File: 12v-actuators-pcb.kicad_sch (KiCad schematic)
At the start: 17 parts, among them J2 3.5mm WR-TBL, J3 690367280676, J5 65100516121, J7 RGBA_LEDs, J8 CAN, U1 MCP2551-I-SN

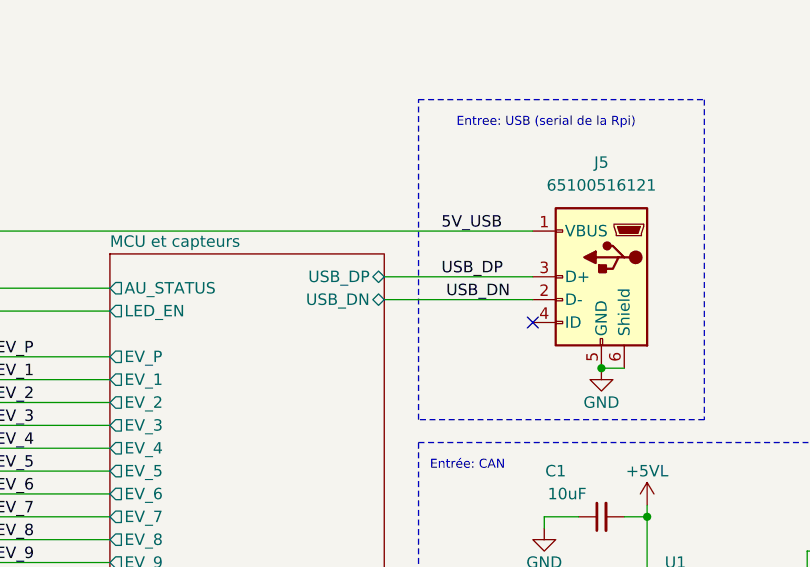
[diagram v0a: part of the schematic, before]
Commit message: debut du tracee des pistes (et modification de l'empreinte R_0402_1005Metric_jumperClosed.kicad_mod pour que le DRC accepte de la router
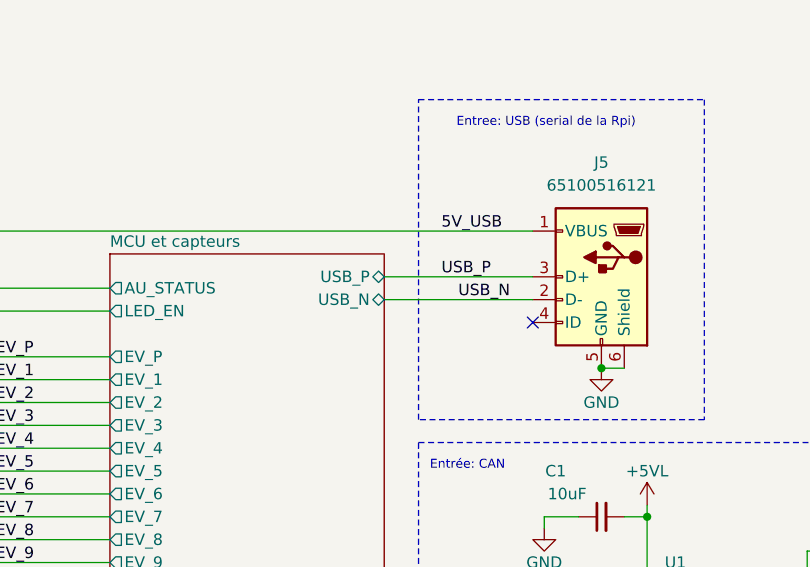
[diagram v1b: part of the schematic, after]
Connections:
- net USB_DN renamed USB_N
- net USB_DP renamed USB_P
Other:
- sheet MCU et capteurs ports: added USB_N, USB_P; removed USB_DN, USB_DP
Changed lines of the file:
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@@
 		)
 	)
-	(label "USB_DN"
+	(label "USB_N"
 		(at 193.04 74.93 180)
 		(effects
@@
 		)
 	)
-	(label "USB_DP"
+	(label "USB_P"
 		(at 185.42 72.39 0)
 		(effects
@@
 			)
 		)
-		(pin "USB_DP" bidirectional
+		(pin "USB_P" bidirectional
 			(at 179.07 72.39 0)
 			(effects
@@
 			)
 		)
-		(pin "USB_DN" bidirectional
+		(pin "USB_N" bidirectional
 			(at 179.07 74.93 0)
 			(effects

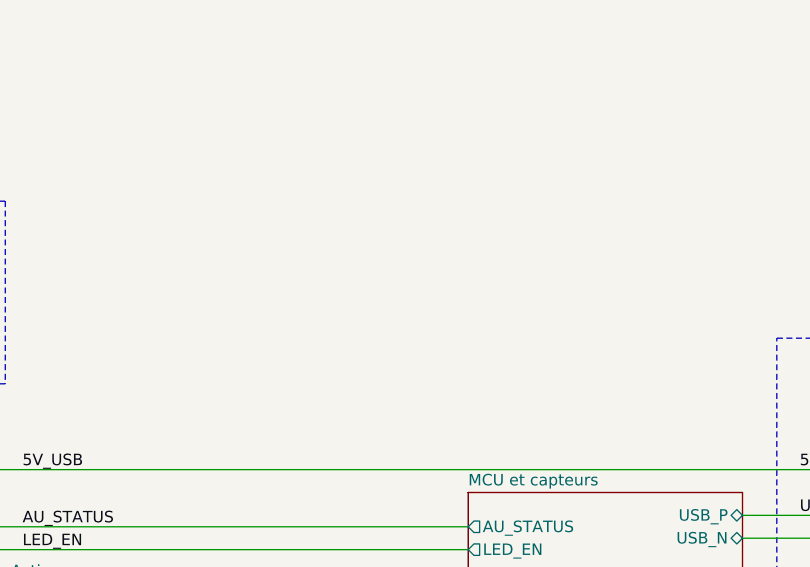
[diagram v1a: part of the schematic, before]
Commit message: WIP ajout des carte Mini-PAMI au routage (todo: finir routage, repeter, associer ref JLCPCB, enregistrer empreinte OPB620 et TRIMM)
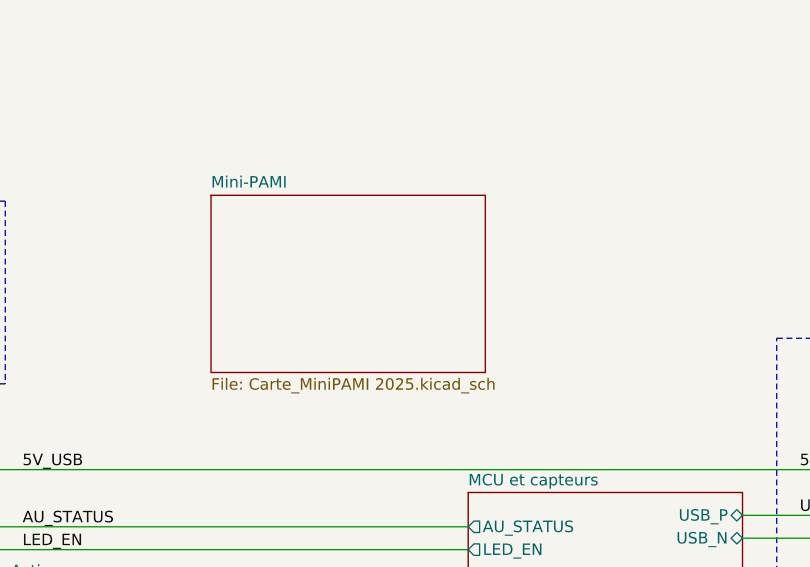
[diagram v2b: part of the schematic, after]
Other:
- added sheet Mini-PAMI (Carte_MiniPAMI 2025.kicad_sch)
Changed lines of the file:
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@@
+	)
+	(sheet
+		(at 120.015 36.83)
+		(size 30.48 19.685)
+		(fields_autoplaced yes)
+		(stroke
+			(width 0.1524)
+			(type solid)
+		)
+		(fill
+			(color 0 0 0 0.0000)
+		)
+		(property "Sheetname" "Mini-PAMI"
+			(at 120.015 36.1184 0)
+			(effects
+				(font
+					(size 1.27 1.27)
+				)
+				(justify left bottom)
+			)
+		)
+		(property "Sheetfile" "Carte_MiniPAMI 2025.kicad_sch"
+			(at 120.015 57.0996 0)
+			(effects
+				(font
+					(size 1.27 1.27)
+				)
+				(justify left top)
+			)
+		)
+		(instances
+			(project "12v-actuators-pcb"
+				(path "/d0b6cc72-ff07-4f5e-a148-04b65c86a715"
+					(page "5")
+				)
+			)
+		)
 	)
 	(sheet

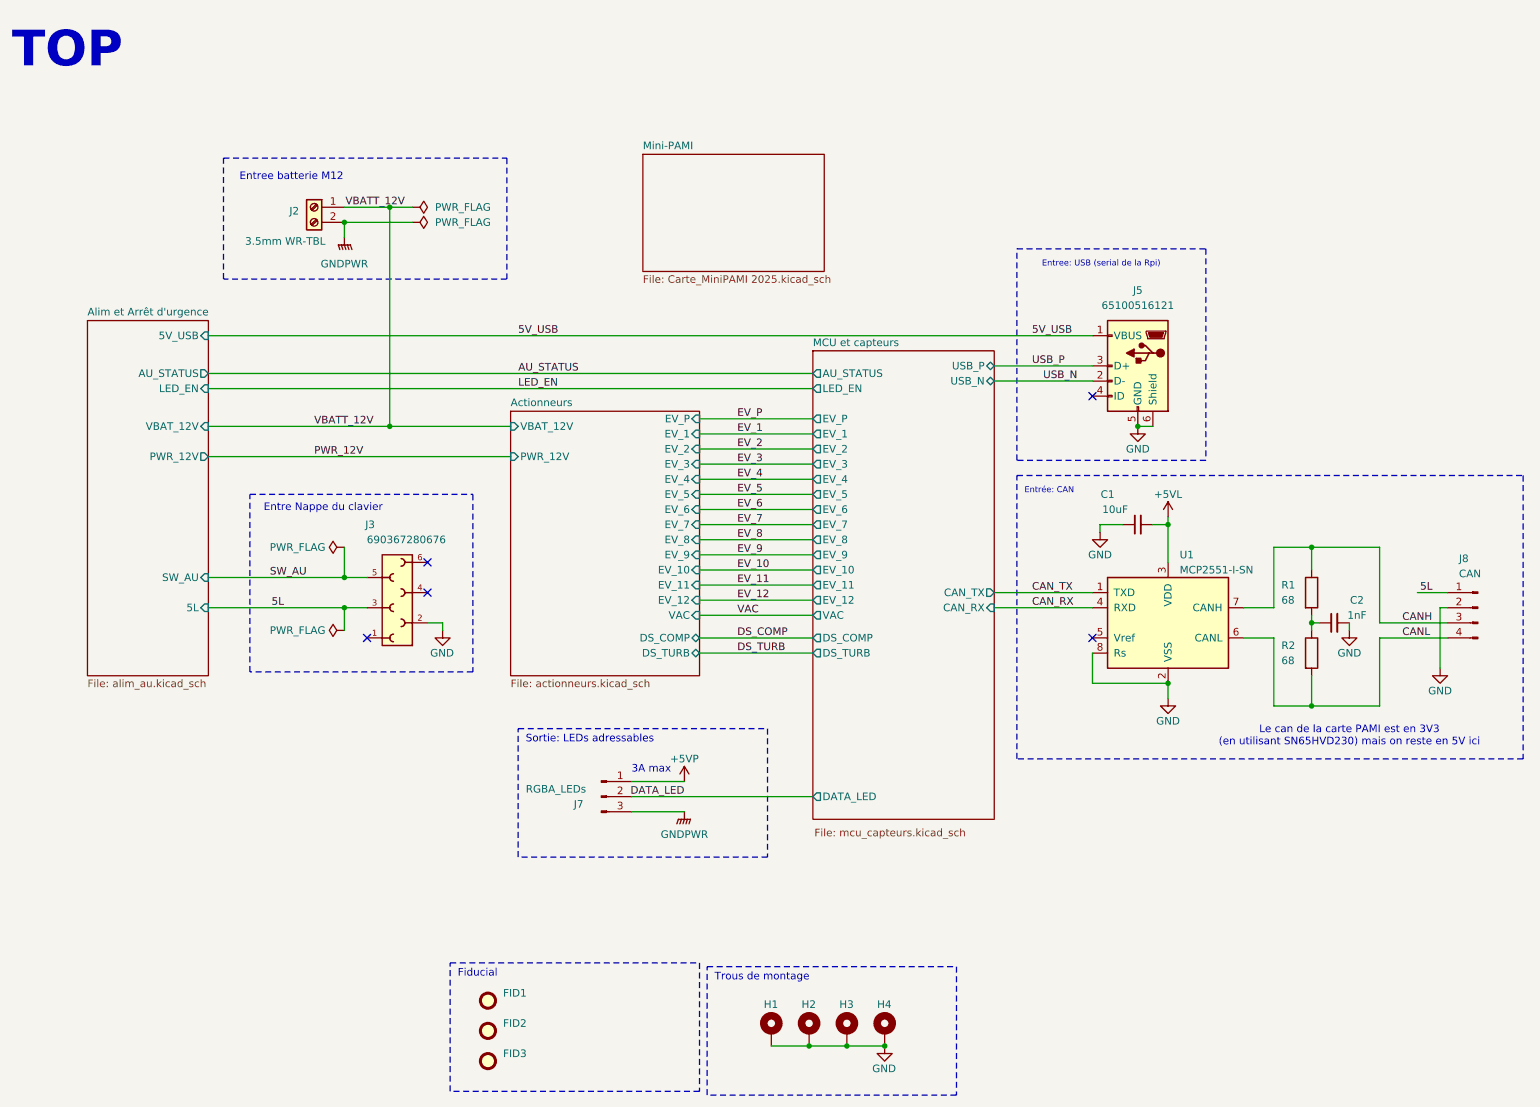
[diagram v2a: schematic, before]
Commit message: corrrection footprint trim, ajout R64, config JLCPCB ASSY, fin panelisation (TODO: revue et cmd)
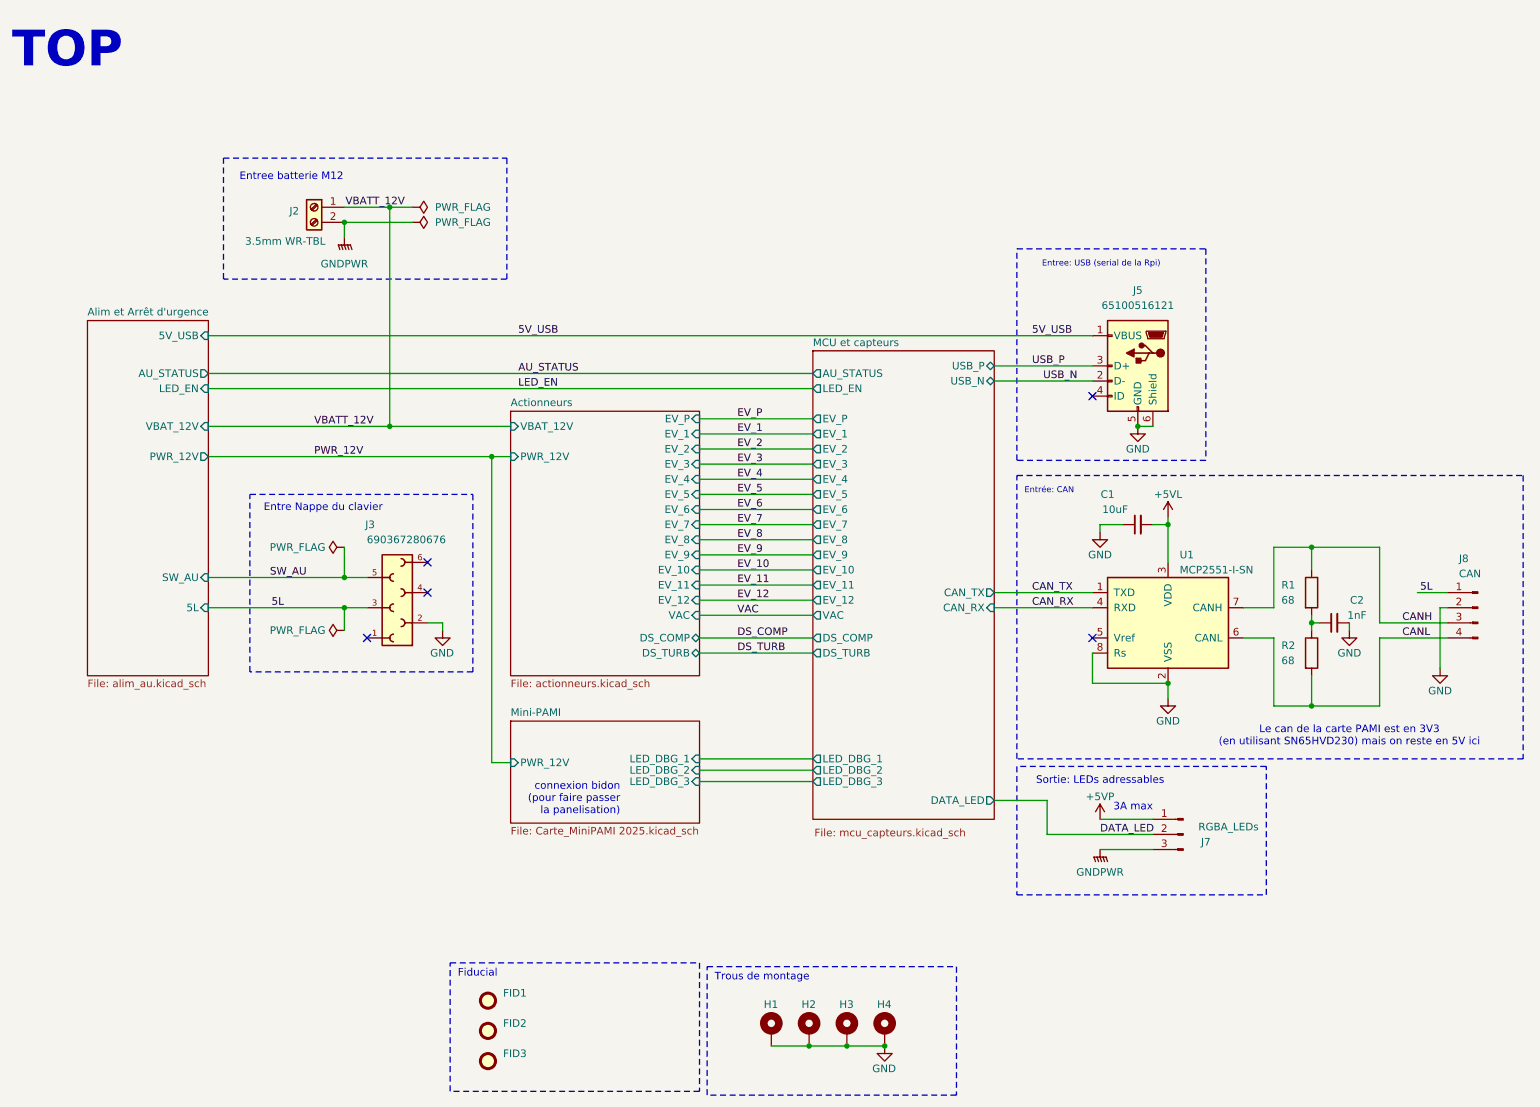
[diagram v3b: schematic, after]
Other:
- sheet MCU et capteurs ports: added LED_DBG_1, LED_DBG_2, LED_DBG_3; removed none
- sheet Mini-PAMI ports: added LED_DBG_1, LED_DBG_2, LED_DBG_3, PWR_12V; removed none
- note added: "connexion bidon (pour faire passer la panelisation)"
- moved on the sheet: J7
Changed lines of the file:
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@@
 	)
 	(junction
+		(at 94.615 87.63)
+		(diameter 0)
+		(color 0 0 0 0)
+	)
+	(junction
 		(at 69.85 48.26)
 		(diameter 0)
@@
 	(wire
 		(pts
+			(xy 187.96 145.415) (xy 179.07 145.415)
+		)
+		(stroke
+			(width 0)
+			(type default)
+		)
+	)
+	(wire
+		(pts
 			(xy 129.54 86.36) (xy 148.59 86.36)
 		)
@@
 	(wire
 		(pts
-			(xy 118.11 147.32) (xy 127 147.32)
+			(xy 205.74 153.67) (xy 196.85 153.67)
 		)
 		(stroke
@@
 	(wire
 		(pts
+			(xy 97.79 139.065) (xy 94.615 139.065)
+		)
+		(stroke
+			(width 0)
+			(type default)
+		)
+	)
+	(wire
+		(pts
 			(xy 255.27 113.03) (xy 254 113.03)
 		)
@@
 	(wire
 		(pts
-			(xy 118.11 142.24) (xy 127 142.24)
+			(xy 205.74 148.59) (xy 196.85 148.59)
 		)
 		(stroke
@@
 	(wire
 		(pts
-			(xy 46.99 87.63) (xy 97.79 87.63)
+			(xy 46.99 87.63) (xy 94.615 87.63)
 		)
 		(stroke
@@
 	(wire
 		(pts
-			(xy 118.11 144.78) (xy 148.59 144.78)
+			(xy 205.74 151.13) (xy 187.96 151.13)
 		)
 		(stroke
@@
 	(wire
 		(pts
+			(xy 129.54 138.43) (xy 148.59 138.43)
+		)
+		(stroke
+			(width 0)
+			(type default)
+		)
+	)
+	(wire
+		(pts
 			(xy 129.54 106.68) (xy 148.59 106.68)
 		)
@@
 	(wire
 		(pts
+			(xy 129.54 142.24) (xy 148.59 142.24)
+		)
+		(stroke
+			(width 0)
+			(type default)
+		)
+	)
+	(wire
+		(pts
 			(xy 129.54 109.22) (xy 148.59 109.22)
 		)
@@
 	(wire
 		(pts
+			(xy 94.615 87.63) (xy 97.79 87.63)
+		)
+		(stroke
+			(width 0)
+			(type default)
+		)
+	)
+	(wire
+		(pts
+			(xy 94.615 139.065) (xy 94.615 87.63)
+		)
+		(stroke
+			(width 0)
+			(type default)
+		)
+	)
+	(wire
+		(pts
+			(xy 129.54 140.335) (xy 148.59 140.335)
+		)
+		(stroke
+			(width 0)
+			(type default)
+		)
+	)
+	(wire
+		(pts
 			(xy 46.99 76.2) (xy 148.59 76.2)
 		)
@@
 	(wire
 		(pts
+			(xy 187.96 151.13) (xy 187.96 145.415)
+		)
+		(stroke
+			(width 0)
+			(type default)
+		)
+	)
+	(wire
+		(pts
 			(xy 129.54 81.28) (xy 148.59 81.28)
 		)
@@
 	)
 	(rectangle
-		(start 99.06 133.35)
-		(end 140.97 154.94)
+		(start 224.79 139.7)
+		(end 182.88 161.29)
 		(stroke
 			(width 0)
@@
 	(text "Sortie: LEDs adressables"
 		(exclude_from_sim no)
-		(at 100.33 135.89 0)
+		(at 207.645 142.875 0)
 		(effects
 			(font
 				(size 1.27 1.27)
 			)
-			(justify left bottom)
+			(justify right bottom)
 		)
 	)
@@
 	(text "3A max"
 		(exclude_from_sim no)
-		(at 118.11 140.97 0)
+		(at 205.74 147.32 0)
 		(effects
 			(font
 				(size 1.27 1.27)
 			)
-			(justify left bottom)
+			(justify right bottom)
 		)
 	)
@@
 		)
 	)
+	(text "connexion bidon\n(pour faire passer\nla panelisation)"
+		(exclude_from_sim no)
+		(at 116.205 147.955 0)
+		(effects
+			(font
+				(size 1.27 1.27)
+			)
+			(justify right bottom)
+		)
+	)
 	(label "EV_7"
 		(at 135.89 99.06 0)
@@
 	)
 	(label "DATA_LED"
-		(at 127 144.78 180)
+		(at 196.85 151.13 0)
 		(effects
 			(font
 				(size 1.27 1.27)
 			)
-			(justify right bottom)
+			(justify left bottom)
 		)
 	)
@@
 	(symbol
 		(lib_id "power:+5VP")
-		(at 127 142.24 0)
+		(at 196.85 148.59 0)
+		(mirror y)
 		(unit 1)
 		(exclude_from_sim no)
@@
 		(fields_autoplaced yes)
 		(property "Reference" "#PWR22"
-			(at 127 146.05 0)
+			(at 196.85 152.4 0)
 			(effects
 				(font
@@
 		)
 		(property "Value" "+5VP"
-			(at 127 138.43 0)
+			(at 196.85 144.78 0)
 			(effects
 				(font
@@
 		)
 		(property "Footprint" ""
-			(at 127 142.24 0)
+			(at 196.85 148.59 0)
 			(effects
 				(font
@@
 		)
 		(property "Datasheet" ""
-			(at 127 142.24 0)
+			(at 196.85 148.59 0)
 			(effects
 				(font
@@
 		)
 		(property "Description" ""
-			(at 127 142.24 0)
+			(at 196.85 148.59 0)
 			(effects
 				(font
@@
 	(symbol
 		(lib_id "Connector:Conn_01x03_Pin")
-		(at 113.03 144.78 0)
+		(at 210.82 151.13 0)
+		(mirror y)
 		(unit 1)
 		(exclude_from_sim no)
@@
 		(dnp no)
 		(property "Reference" "J7"
-			(at 109.22 146.05 0)
+			(at 214.63 152.4 0)
 			(effects
 				(font
@@
 		)
 		(property "Value" "RGBA_LEDs"
-			(at 105.41 143.51 0)
+			(at 218.44 149.86 0)
 			(effects
 				(font
@@
 		)
 		(property "Footprint" "Connector_PinHeader_2.54mm:PinHeader_1x03_P2.54mm_Vertical"
-			(at 113.03 144.78 0)
+			(at 210.82 151.13 0)
 			(effects
 				(font
@@
 		)
 		(property "Datasheet" "~"
-			(at 113.03 144.78 0)
+			(at 210.82 151.13 0)
 			(effects
 				(font
@@
 		)
 		(property "Description" ""
-			(at 113.03 144.78 0)
+			(at 210.82 151.13 0)
 			(effects
 				(font
@@
 	(symbol
 		(lib_id "power:GNDPWR")
-		(at 127 147.32 0)
+		(at 196.85 153.67 0)
+		(mirror y)
 		(unit 1)
 		(exclude_from_sim no)
@@
 		(dnp no)
 		(property "Reference" "#PWR24"
-			(at 127 152.4 0)
+			(at 196.85 158.75 0)
 			(effects
 				(font
@@
 		)
 		(property "Value" "GNDPWR"
-			(at 127 151.13 0)
+			(at 196.85 157.48 0)
 			(effects
 				(font
@@
 		)
 		(property "Footprint" ""
-			(at 127 148.59 0)
+			(at 196.85 154.94 0)
 			(effects
 				(font
@@
 		)
 		(property "Datasheet" ""
-			(at 127 148.59 0)
+			(at 196.85 154.94 0)
 			(effects
 				(font
@@
 		)
 		(property "Description" ""
-			(at 127 147.32 0)
+			(at 196.85 153.67 0)
 			(effects
 				(font
@@
 	)
 	(sheet
-		(at 120.015 36.83)
-		(size 30.48 19.685)
+		(at 97.79 132.08)
+		(size 31.75 17.145)
 		(fields_autoplaced yes)
 		(stroke
@@
 		)
 		(property "Sheetname" "Mini-PAMI"
-			(at 120.015 36.1184 0)
+			(at 97.79 131.3684 0)
 			(effects
 				(font
@@
 		)
 		(property "Sheetfile" "Carte_MiniPAMI 2025.kicad_sch"
-			(at 120.015 57.0996 0)
+			(at 97.79 149.8096 0)
 			(effects
 				(font
@@
 			)
 		)
+		(pin "LED_DBG_1" input
+			(at 129.54 138.43 0)
+			(effects
+				(font
+					(size 1.27 1.27)
+				)
+				(justify right)
+			)
+		)
+		(pin "LED_DBG_3" input
+			(at 129.54 142.24 0)
+			(effects
+				(font
+					(size 1.27 1.27)
+				)
+				(justify right)
+			)
+		)
+		(pin "LED_DBG_2" input
+			(at 129.54 140.335 0)
+			(effects
+				(font
+					(size 1.27 1.27)
+				)
+				(justify right)
+			)
+		)
+		(pin "PWR_12V" input
+			(at 97.79 139.065 180)
+			(effects
+				(font
+					(size 1.27 1.27)
+				)
+				(justify left)
+			)
+		)
 		(instances
 			(project "12v-actuators-pcb"
@@
 		)
 		(pin "DATA_LED" output
-			(at 148.59 144.78 180)
+			(at 179.07 145.415 0)
 			(effects
 				(font
 					(size 1.27 1.27)
 				)
-				(justify left)
+				(justify right)
 			)
 		)
@@
 			(effects
 				(font
+					(size 1.27 1.27)
+				)
+				(justify left)
+			)
+		)
+		(pin "LED_DBG_2" output
+			(at 148.59 140.335 180)
+			(effects
+				(font
+					(size 1.27 1.27)
+				)
+				(justify left)
+			)
+		)
+		(pin "LED_DBG_3" output
+			(at 148.59 142.24 180)
+			(effects
+				(font
+					(size 1.27 1.27)
+				)
+				(justify left)
+			)
+		)
+		(pin "LED_DBG_1" output
+			(at 148.59 138.43 180)
+			(effects
+				(font
